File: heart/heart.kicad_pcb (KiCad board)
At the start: 4 copper layers, 133 parts, among them J1 BatteryPort, J10 TYPE-C-31-M-12, J2 Leg_L, J3 Arm_L, J4 Head, J5 SWD_DBG, J6 SWD_DBG_PIN, J7 Arm_R, J8 Leg_R, J9 Cerebellum, Q1 BSC0702LS, Q2 2301, Q3 2N7002, Q4 NTMFS5C670NLT1G, Q5 NTMFS5C670NLT1G, Q6 2301, Q7 2N7002, Q8 NTMFS5C670NLT1G, Q9 NTMFS5C670NLT1G, U1 AMS1117-3.3, U2 TJA1042T, U3 TPS54231, U4 IP2368, U5 GD32C103TBUx, Y1 8M

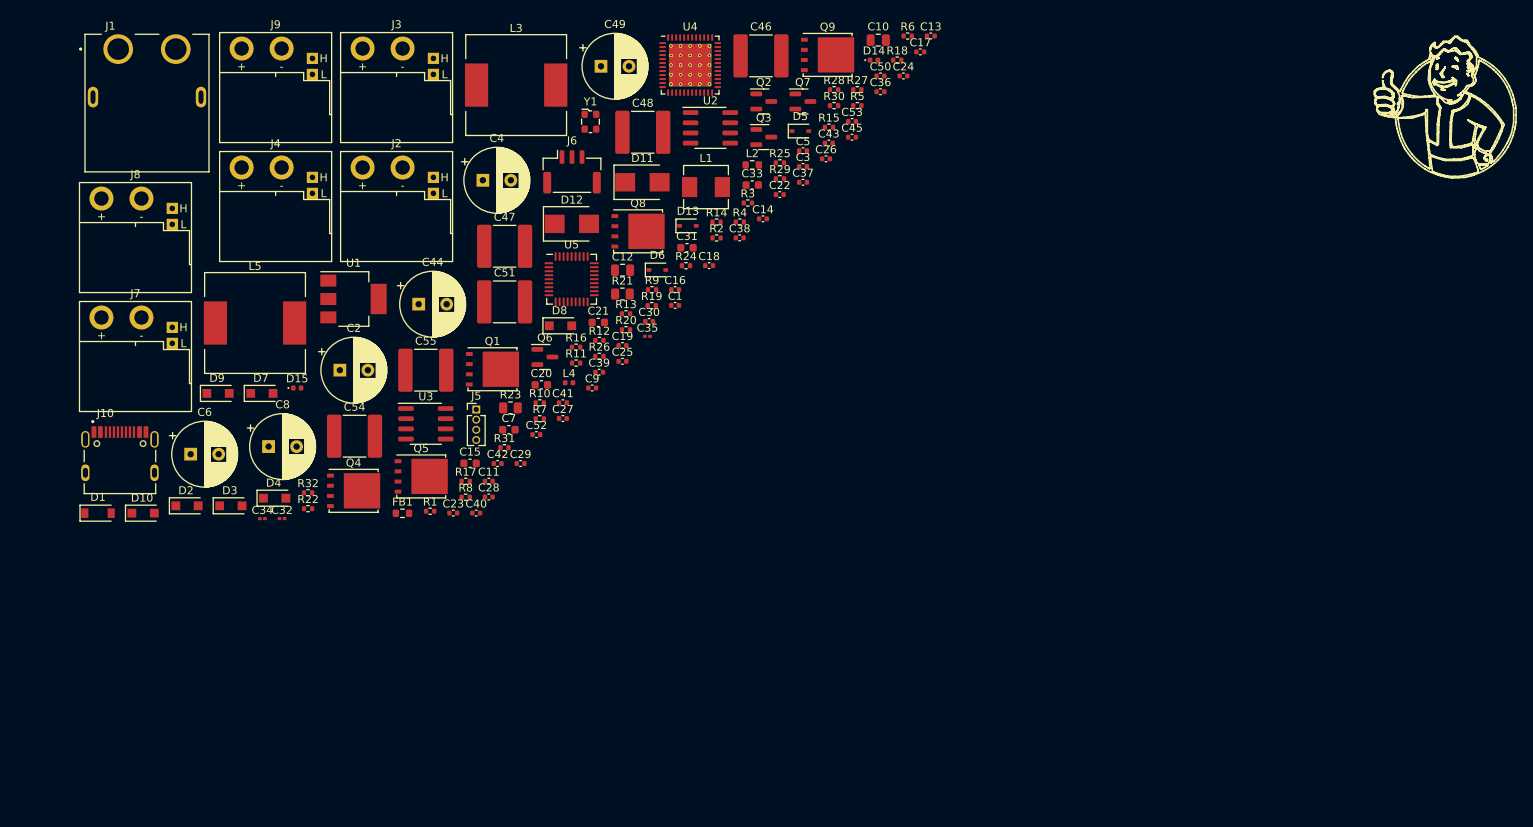
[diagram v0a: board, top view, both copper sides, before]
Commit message: [New] Complete Heart board v2.0
1. There are two XT60 ports on heart board, one for power input, one for power output.
2. There is a 4pin GH 1.25 port, designed for CAN FD(1.CAN_H, 2.CAN_H, 3.CAN_L, 4.CAN_L)
3. USB Type C port is designed for PD charging.
4. Also there is a SWD port for flashing and debugging.
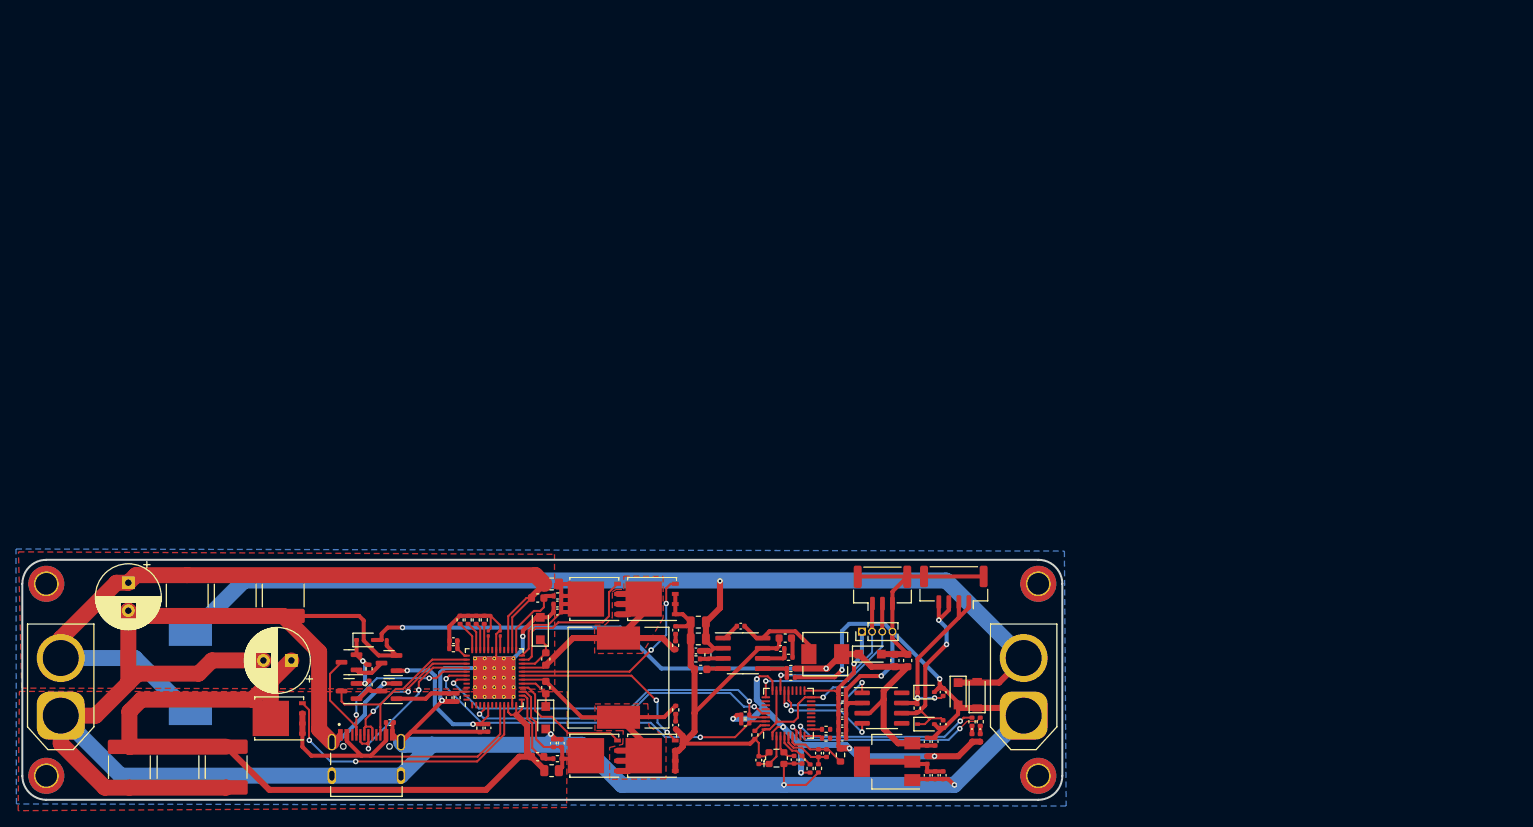
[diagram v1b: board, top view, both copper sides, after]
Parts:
- removed C12: 4.7uF 50V, Capacitor_SMD:C_0805_2012Metric
- removed C9: 10uf 50V, Capacitor_SMD:C_0402_1005Metric
- removed D11, D12: SMF30A, Diode_SMD:D_SMB
- removed D13: 1SS355, Diode_SMD:D_SOD-323
- removed D14: 16-213/SDRC/S530-A3/TR8, Diode_SMD:D_0402_1005Metric
- removed D15: 16-213/GHC-YR1S1/3T, Diode_SMD:D_0402_1005Metric
- removed FB1: 220R, Resistor_SMD:R_0603_1608Metric
- removed J10: TYPE-C-31-M-12, Rolling_Custom:HRO_TYPE-C-31-M-12
- removed J6: SWD_DBG_PIN, Connector_JST:JST_GH_SM03B-GHS-TB_1x03-1MP_P1.25mm_Horizontal
- removed J7: Arm_R, Rolling_Custom:XT30PW(2+2)
- removed J9: Cerebellum, Rolling_Custom:XT30PW(2+2)
- removed R31, R32: 2r, Resistor_SMD:R_0402_1005Metric
- added Mount1: MountingHole_2.7mm_M2.5_ISO7380_Pad_TopBottom, MountingHole:MountingHole_2.7mm_M2.5_ISO7380_Pad_TopBottom, F.Cu at (66.0, 126.8)
- added Mount1: MountingHole_2.7mm_M2.5_ISO7380_Pad_TopBottom, MountingHole:MountingHole_2.7mm_M2.5_ISO7380_Pad_TopBottom, F.Cu at (190.0, 150.8)
- added Mount1: MountingHole_2.7mm_M2.5_ISO7380_Pad_TopBottom, MountingHole:MountingHole_2.7mm_M2.5_ISO7380_Pad_TopBottom, F.Cu at (66.0, 150.8)
- added Mount1: MountingHole_2.7mm_M2.5_ISO7380_Pad_TopBottom, MountingHole:MountingHole_2.7mm_M2.5_ISO7380_Pad_TopBottom, F.Cu at (190.0, 126.8)
- C19: value 100nF, 10%, 10V -> 47uf 50V; footprint Capacitor_SMD:C_0402_1005Metric -> Capacitor_SMD:C_0603_1608Metric
- C2, C8: value 100uf -> 10uf 50V; footprint Capacitor_THT:CP_Radial_D8.0mm_P3.50mm -> Capacitor_SMD:C_0402_1005Metric
- C20: value 47uf 50V -> 100nF, 10%, 10V; footprint Capacitor_SMD:C_0603_1608Metric -> Capacitor_SMD:C_0402_1005Metric
- C3: value 10uf 50V -> 1.5nf 50V; footprint Capacitor_SMD:C_0402_1005Metric -> Capacitor_SMD:C_0603_1608Metric
- C36: value 10uF, 10%, 10V -> 100nF, 10%, 50V
- C38: value 100nF, 10%, 50V -> 10uF, 10%, 10V
- C39: value 100nF, 10%, 10V -> 100nF, 10%, 50V
- C4: value 100uf -> 100nF, 10%, 50V; footprint Capacitor_THT:CP_Radial_D8.0mm_P3.50mm -> Capacitor_SMD:C_0402_1005Metric
- C41: value 100nF, 10%, 50V -> 100nF, 10%, 10V
- C43: value 10uF, 10%, 10V -> 220uf; footprint Capacitor_SMD:C_0402_1005Metric -> Capacitor_THT:CP_Radial_D8.0mm_P3.50mm
- C44: value 220uf -> 10uF, 10%, 10V; footprint Capacitor_THT:CP_Radial_D8.0mm_P3.50mm -> Capacitor_SMD:C_0402_1005Metric
- C45: value 100nF, 10%, 10V -> 22uF,50V; footprint Capacitor_SMD:C_0402_1005Metric -> Capacitor_SMD:C_2220_5650Metric
- C46: value 22uF,50V -> 100nF, 10%, 10V; footprint Capacitor_SMD:C_2220_5650Metric -> Capacitor_SMD:C_0402_1005Metric
- C5: value 100nF, 10%, 50V -> 100nF, 10%, 100V; footprint Capacitor_SMD:C_0402_1005Metric -> Capacitor_SMD:C_0603_1608Metric
- C6: value 100uf -> 100nF, 10%, 100V; footprint Capacitor_THT:CP_Radial_D8.0mm_P3.50mm -> Capacitor_SMD:C_0603_1608Metric
- C7: value 1.5nf 50V -> 4.7uF 50V; footprint Capacitor_SMD:C_0603_1608Metric -> Capacitor_SMD:C_0805_2012Metric
- D10: value BZT52C5V1S -> 16-213/GHC-YR1S1/3T; footprint Diode_SMD:D_SOD-123F -> Diode_SMD:D_0402_1005Metric
- D3, D4: value BZT52C24 -> 12V; footprint Diode_SMD:D_SOD-123F -> Diode_SMD:D_SOD-323
- D5: value 12V -> BZT52C5V1S; footprint Diode_SMD:D_SOD-323 -> Diode_SMD:D_SOD-123F
- D6: value 12V -> SMF30A; footprint Diode_SMD:D_SOD-323 -> Diode_SMD:D_SOD-123F
- D7: value BZT52C24 -> SMF30A
- D8: value BZT52C24 -> 1SS355; footprint Diode_SMD:D_SOD-123F -> Diode_SMD:D_SOD-323
- D9: value BZT52C24 -> 16-213/SDRC/S530-A3/TR8; footprint Diode_SMD:D_SOD-123F -> Diode_SMD:D_0402_1005Metric
- J1: footprint Rolling_Custom:AMASS_XT60PW-F -> Connector_AMASS:AMASS_XT60-F_1x02_P7.20mm_Vertical
- J2: value Leg_L -> PowerOutput; footprint Rolling_Custom:XT30PW(2+2) -> Connector_AMASS:AMASS_XT60-F_1x02_P7.20mm_Vertical
- J3: value Arm_L -> CAN FD; footprint Rolling_Custom:XT30PW(2+2) -> Connector_JST:JST_GH_SM04B-GHS-TB_1x04-1MP_P1.25mm_Horizontal
- J4: value Head -> SWD_DBG; footprint Rolling_Custom:XT30PW(2+2) -> Connector_PinHeader_1.27mm:PinHeader_1x04_P1.27mm_Vertical
- J5: value SWD_DBG -> SWD_DBG_Mounting; footprint Connector_PinHeader_1.27mm:PinHeader_1x04_P1.27mm_Vertical -> Connector_JST:JST_GH_BM03B-GHS-TBT_1x03-1MP_P1.25mm_Vertical
- J8: value Leg_R -> TYPE-C-31-M-12; footprint Rolling_Custom:XT30PW(2+2) -> Rolling_Custom:HRO_TYPE-C-31-M-12
- L1: value 15uh, SLO0530H150MTT -> LQW15AN1N3D10D; footprint Inductor_SMD:L_Sunlord_MWSA0518_5.4x5.2mm -> Inductor_SMD:L_0402_1005Metric
- L2: value FCM1608KF-100T07 -> 15uh, SLO0530H150MTT; footprint Resistor_SMD:R_0603_1608Metric -> Inductor_SMD:L_Sunlord_MWSA0518_5.4x5.2mm
- L3: moved to B.Cu
- L4: value LQW15AN1N3D10D -> FCM1608KF-100T07; footprint Inductor_SMD:L_0402_1005Metric -> Resistor_SMD:R_0603_1608Metric
- R16, R17: value 1k -> 0
- R18: value 0 -> 10r
- R19: value 0 -> 0.005r; footprint Resistor_SMD:R_0402_1005Metric -> Resistor_SMD:R_0805_2012Metric
- R22: value 10r -> 10k
- R23: value 0.005r -> 1M; footprint Resistor_SMD:R_0805_2012Metric -> Resistor_SMD:R_0402_1005Metric
- R24: value 10k -> 0
- R25: value 1M -> 10k
- R26: value 0 -> 330r
- R28: value 330r -> 1M
- R29: value 10k -> 2r
- R30: value 1M -> 2r
- U1: value AMS1117-3.3 -> TJA1042T; footprint Package_TO_SOT_SMD:SOT-223-3_TabPin2 -> Package_SO:SOIC-8_3.9x4.9mm_P1.27mm
- U2: value TJA1042T -> AMS1117-3.3; footprint Package_SO:SOIC-8_3.9x4.9mm_P1.27mm -> Package_TO_SOT_SMD:SOT-223-3_TabPin2
- moved D1 112.2 mm to (182.3, 140.7), turned to 90 degrees
- moved C45 111.0 mm to (88.5, 149.7), turned to -90 degrees
- moved D10 107.4 mm to (181.7, 146.0), turned to -90 degrees
- moved D9 104.5 mm to (182.7, 146.0), turned to -90 degrees
- moved J2 104.1 mm to (188.2, 143.3), turned to 90 degrees
- moved C48 102.1 mm to (76.4, 149.7), turned to -90 degrees
- moved D2 99.2 mm to (180.0, 140.6), turned to -90 degrees
- moved J3 96.9 mm to (179.4, 127.2), turned to 180 degrees
- moved C50 94.6 mm to (116.3, 141.0), turned to -90 degrees
- moved J4 93.5 mm to (167.9, 132.8), turned to 90 degrees
- moved C43 93.2 mm to (96.6, 136.4), turned to 180 degrees
- moved C13 92.4 mm to (178.1, 150.7), turned to -90 degrees
- moved C8 92.0 mm to (176.1, 150.7), turned to -90 degrees
- moved D3 91.1 mm to (175.9, 144.3)
- moved C36 90.7 mm to (130.4, 146.7), turned to 90 degrees
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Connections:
- C19 pad 1: NRST -> +5V
- C2 pad 1: +24V -> +5V
- C2 pad 2: GNDA -> GND
- C20 pad 1: +5V -> NRST
- C3 pad 1: +5V -> Net-(C3-Pad1)
- C36 pad 1: GND -> Net-(C36-Pad1)
- C36 pad 2: +3V3 -> GND
- C38 pad 1: Net-(C38-Pad1) -> GND
- C38 pad 2: GND -> +3V3
- C39 pad 1: GND -> Net-(C36-Pad1)
- C39 pad 2: +3V3 -> GND
- C4 pad 1: +24V -> +5V
- C4 pad 2: GNDA -> GND
- C41 pad 1: Net-(C38-Pad1) -> GND
- C41 pad 2: GND -> +3V3
- C43 pad 1: VREF_S -> USB_VBUS_D
- C43 pad 2: VREF_D -> GND
- C44 pad 1: USB_VBUS_D -> VREF-
- C44 pad 2: GND -> VREF+
- C45 pad 1: VREF_S -> USB_VBUS_D
- C45 pad 2: VREF_D -> GND
- C46 pad 1: USB_VBUS_D -> VREF-
- C46 pad 2: GND -> VREF+
- C5 pad 1: +5V -> BST1
- C5 pad 2: GND -> BST1C
- C6 pad 1: +24V -> BST2
- C6 pad 2: GNDA -> BST2C
- C7 pad 1: Net-(C7-Pad1) -> +24V
- C8 pad 1: +24V -> Net-(C11-Pad1)
- C8 pad 2: GNDA -> GND
- D1 pad 1: GNDA -> GND
- D10 pad 1: +5V -> Net-(D10-Pad1)
- D10 pad 2: GND -> +3V3
- D2 pad 2: GNDA -> GND
- D3 pad 1: +24V -> CANFD_L
- D3 pad 2: GNDA -> GND
- D4 pad 1: +24V -> CANFD_H
- D4 pad 2: GNDA -> GND
- D5 pad 1: CANFD_L -> +5V
- D6 pad 1: CANFD_H -> BST2
- D7 pad 1: +24V -> BST1
- D7 pad 2: GNDA -> GND
- D8 pad 1: +24V -> Net-(D8-Pad1)
- D8 pad 2: GNDA -> +5V
- D9 pad 1: +24V -> Net-(D9-Pad1)
- D9 pad 2: GNDA -> +3V3
- J1 pad 1: +BATT -> GND
- J1 pad 2: GNDA -> +BATT
- J2 pad 1: +24V -> GND
- J2 pad 2: GNDA -> +24V
- J3 pad 1: +24V -> CANFD_H
- J3 pad 2: GNDA -> CANFD_H
- J3 pad 3: CANFD_H -> CANFD_L
- J4 pad 1: +24V -> +3V3
- J4 pad 2: GNDA -> SWDIO
- J4 pad 3: CANFD_H -> SWCLK
- J4 pad 4: CANFD_L -> GND
- J5 pad 1: +3V3 -> SWDIO
- J5 pad 2: SWDIO -> SWCLK
- J5 pad 3: SWCLK -> GND
- L1 pad 1: +5V -> Net-(C11-Pad1)
- L1 pad 2: Net-(C18-Pad1) -> +3V3
- L2 pad 1: +3V3 -> +5V
- L2 pad 2: VREF_D -> Net-(C18-Pad1)
- L3 pad 1: BST2C -> +BATT
- L3 pad 2: BST1C -> +24V
- L4 pad 1: Net-(C11-Pad1) -> +3V3
- L4 pad 2: +3V3 -> VREF+
- L5 pad 1: +BATT -> BST2C
- L5 pad 2: +24V -> BST1C
- Q2 pad 2: Net-(D13-Pad1) -> Net-(D8-Pad1)
- Q4 pad 5: Net-(C37-Pad1) -> Net-(C36-Pad1)
- Q5 pad 5: Net-(C38-Pad1) -> Net-(C37-Pad1)
- Q6 pad 2: Net-(D13-Pad1) -> Net-(D8-Pad1)
- R1 pad 2: Net-(C7-Pad1) -> Net-(C3-Pad1)
- R16 pad 1: BAT_MODE -> Net-(R16-Pad1)
- R16 pad 2: GND -> unconnected-(R16-Pad2)
- R17 pad 2: GND -> unconnected-(R17-Pad2)
- R18 pad 1: Net-(R18-Pad1) -> Net-(C37-Pad1)
- R18 pad 2: unconnected-(R18-Pad2) -> Net-(C31-Pad1)
- R19 pad 1: Net-(R19-Pad1) -> +BATT
- R19 pad 2: unconnected-(R19-Pad2) -> Net-(C37-Pad1)
- R20 pad 1: Net-(C38-Pad1) -> Net-(C36-Pad1)
- R20 pad 2: Net-(C31-Pad1) -> Net-(C33-Pad2)
- R21 pad 1: +BATT -> USB_VBUS_D
- R21 pad 2: Net-(C38-Pad1) -> Net-(C36-Pad1)
- R22 pad 1: Net-(C37-Pad1) -> Net-(Q2-Pad1)
- R22 pad 2: Net-(C33-Pad2) -> Net-(D8-Pad1)
- R23 pad 1: USB_VBUS_D -> GND
- R23 pad 2: Net-(C37-Pad1) -> HLED
- R24 pad 1: Net-(Q2-Pad1) -> GND
- R24 pad 2: Net-(D13-Pad1) -> VREF-
- R25 pad 1: GND -> Net-(Q6-Pad1)
- R25 pad 2: HLED -> Net-(D8-Pad1)
- R26 pad 1: GND -> LED_RED
- R26 pad 2: VREF_S -> Net-(D9-Pad1)
- R27 pad 1: LED_RED -> LED_GREEN
- R27 pad 2: Net-(D14-Pad1) -> Net-(D10-Pad1)
- R28 pad 1: LED_GREEN -> GND
- R28 pad 2: Net-(D15-Pad1) -> BAT_MODE
- R29 pad 1: Net-(Q6-Pad1) -> BST1C
- R29 pad 2: Net-(D13-Pad1) -> Net-(C52-Pad1)
- R30 pad 1: GND -> BST2C
- R30 pad 2: BAT_MODE -> Net-(C53-Pad1)
- U1 pad 1: GND -> CANFD_TX
- U1 pad 2: Net-(C11-Pad1) -> GND
- U2 pad 1: CANFD_TX -> GND
- U2 pad 2: GND -> Net-(C11-Pad1)
- U4 pad 15: Net-(C37-Pad1) -> Net-(C36-Pad1)
- U4 pad 17: Net-(D11-Pad1) -> BST1
- U4 pad 22: Net-(D12-Pad1) -> BST2
- U4 pad 24: Net-(C38-Pad1) -> Net-(C37-Pad1)
- U4 pad 47: Net-(R17-Pad1) -> unconnected-(U4-Pad47)
- U5 pad 10: Net-(R19-Pad1) -> Net-(R17-Pad1)
- U5 pad 25: unconnected-(U5-Pad25) -> SWDIO
- U5 pad 28: (no net) -> SWCLK
- U5 pad 29: (no net) -> unconnected-(U5-Pad29)
- U5 pad 9: Net-(R18-Pad1) -> Net-(R16-Pad1)
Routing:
- net GND: track 0.00 -> 531.0 mm, vias 0 -> 10
- net +24V: track 0.00 -> 133.0 mm, vias 0 -> 1
- net +BATT: track 0.00 -> 103.7 mm
- net USB_VBUS_D: track 0.00 -> 100.0 mm
- net +5V: track 0.00 -> 95.0 mm, vias 0 -> 2
- net +3V3: track 0.00 -> 73.5 mm, vias 0 -> 7
- net CH_SDA: track 0.00 -> 47.2 mm, vias 0 -> 2
- net CH_SCL: track 0.00 -> 45.5 mm, vias 0 -> 2
- net USB_VBUS_S: track 0.00 -> 42.5 mm
- net CH_INT: track 0.00 -> 39.7 mm, vias 0 -> 2
- net BST1C: track 0.00 -> 39.0 mm
- net BST2C: track 0.00 -> 38.7 mm
- net Net-(Q1-Pad4): track 0.00 -> 35.5 mm, vias 0 -> 2
- net USB_CC1: track 0.00 -> 30.7 mm, vias 0 -> 2
- net LG2: track 0.00 -> 27.1 mm, vias 0 -> 2
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- added copper zone on F.Cu, net +BATT
- added copper zone on F.Cu, net BST1C
- added copper zone on F.Cu, net BST2C
- added copper zone on B.Cu, net GND
- added copper zone on F.Cu, net USB_VBUS_D
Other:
- board outline added: 130 x 30 mm
- copper layers 4 -> 2

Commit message: [Modify] Change FP of battery power input & SWD
1. Change battery input port to XT60 M vertical.
2. Change SWD port to Horizontal.
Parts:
- J1: footprint Connector_AMASS:AMASS_XT60-F_1x02_P7.20mm_Vertical -> Connector_AMASS:AMASS_XT60-M_1x02_P7.20mm_Vertical
- J5: footprint Connector_JST:JST_GH_BM03B-GHS-TBT_1x03-1MP_P1.25mm_Vertical -> Connector_JST:JST_GH_SM03B-GHS-TB_1x03-1MP_P1.25mm_Horizontal
- turned J5 to 180 degrees
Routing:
- net GND: track 531.0 -> 538.6 mm, vias 10 -> 11
- net SWDIO: track 20.6 -> 27.2 mm

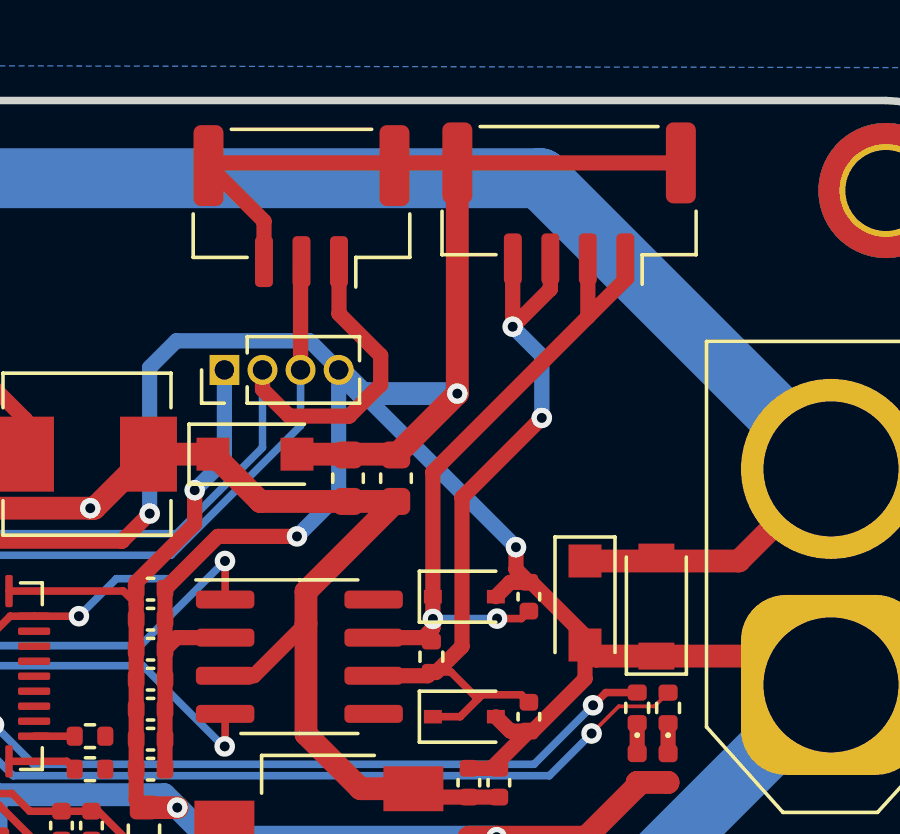
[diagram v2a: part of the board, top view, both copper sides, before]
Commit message: [Fix] Fix XT60 layout & Change CAN ports
1. It seems 2pin is enough for  CAN FD inside the body.
2. Fix XT60 layout.
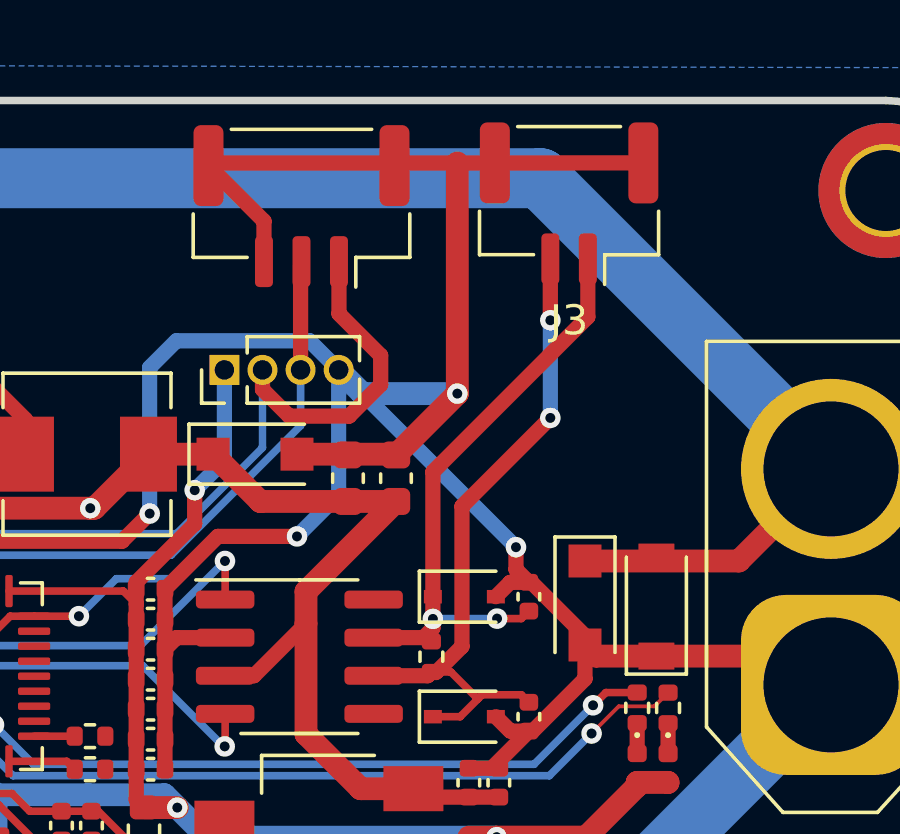
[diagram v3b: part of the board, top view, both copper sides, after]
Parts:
- J3: footprint Connector_JST:JST_GH_SM04B-GHS-TB_1x04-1MP_P1.25mm_Horizontal -> Connector_JST:JST_GH_SM02B-GHS-TB_1x02-1MP_P1.25mm_Horizontal
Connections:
- J3 pad 2: CANFD_H -> CANFD_L
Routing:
- net CANFD_L: track 26.1 -> 23.0 mm
- net CANFD_H: track 22.3 -> 19.9 mm
- net GND: track 538.6 -> 537.3 mm
